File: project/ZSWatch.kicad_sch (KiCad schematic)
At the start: 34 parts, among them IC1 nPM1300-QEXX, IC2 TS3USB221A, IC3 AT25SL128A, M1 NORA-B106, X1 DOCK, X2 INT, X3 VBAT, X4 VBUS, X5 SEL, X6 3V3

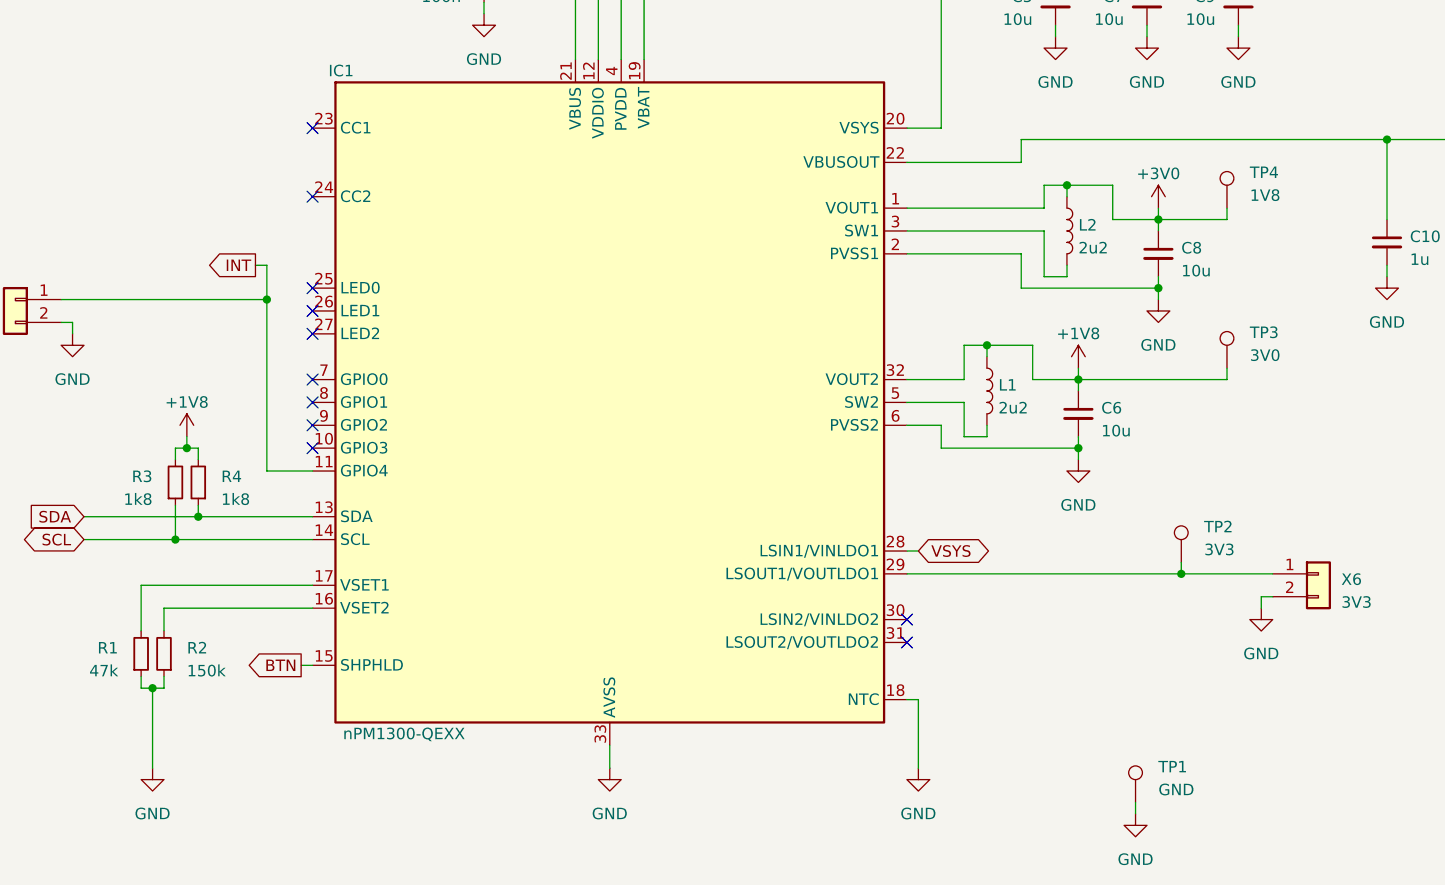
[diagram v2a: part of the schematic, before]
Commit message: Add missing output capacitor for LDO output
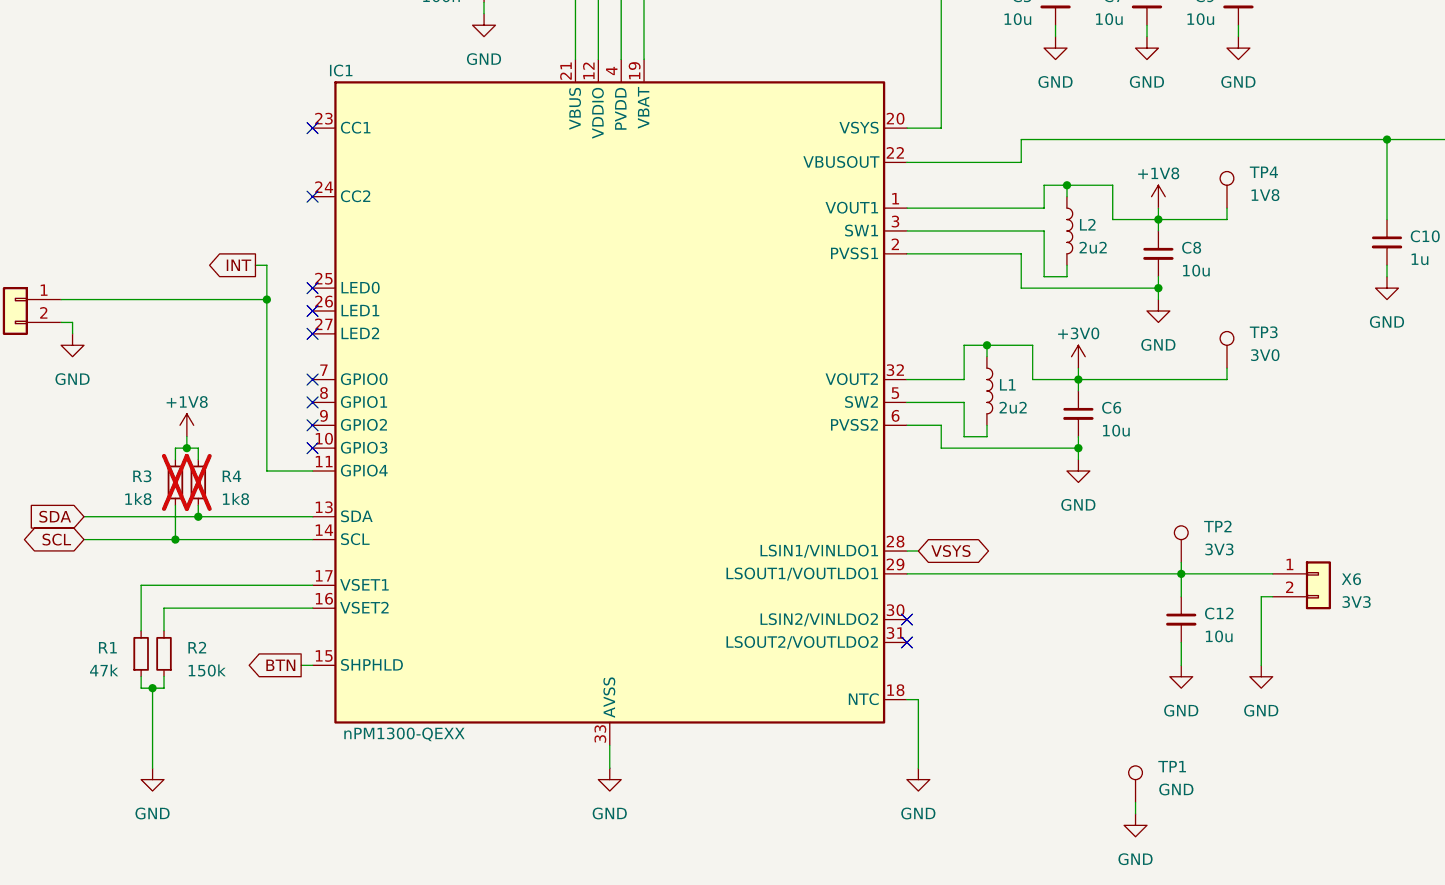
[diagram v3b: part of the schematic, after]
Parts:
- added C12: 10u, Capacitor_SMD:C_0603_1608Metric, symbol Device:C_Small
- R3, R4: now not fitted; now left out of the parts list
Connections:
- net +1V8: now also C8.1, IC1.1 (VOUT1), L2.1, TP4.1; no longer C6.1, IC1.32 (VOUT2), L1.1, TP3.1
- net +3V0: now also C6.1, IC1.32 (VOUT2), L1.1, TP3.1; no longer C8.1, IC1.1 (VOUT1), L2.1, TP4.1
- net GND: now also C12.2
- net at IC1.29 (LSOUT1/VOUTLDO1), TP2.1, X6.1 (Pin_1): now also C12.1
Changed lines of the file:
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@@
     (stroke (width 0) (type default))
   )
-  (wire (pts (xy 161.29 170.18) (xy 161.29 171.45))
+  (wire (pts (xy 161.29 170.18) (xy 161.29 177.8))
     (stroke (width 0) (type default))
   )
@@
     (stroke (width 0) (type default))
   )
+  (wire (pts (xy 152.4 167.64) (xy 152.4 170.18))
+    (stroke (width 0) (type default))
+  )
   (wire (pts (xy 30.48 311.15) (xy 31.75 311.15))
     (stroke (width 0) (type default))
@@
     (stroke (width 0) (type default))
   )
+  (wire (pts (xy 152.4 175.26) (xy 152.4 177.8))
+    (stroke (width 0) (type default))
+  )
   (wire (pts (xy 74.93 96.52) (xy 74.93 97.79))
     (stroke (width 0) (type default))
@@
     )
   )
-  (symbol (lib_id "power:+1V8") (at 140.97 144.78 0) (unit 1)
+  (symbol (lib_id "power:GND") (at 152.4 177.8 0) (unit 1)
+    (in_bom yes) (on_board yes) (dnp no)
+    (property "Reference" "#PWR029" (at 152.4 184.15 0)
+      (effects (font (size 1.27 1.27)) hide)
+    )
+    (property "Value" "GND" (at 152.4 182.88 0)
+      (effects (font (size 1.27 1.27)))
+    )
+    (property "Footprint" "" (at 152.4 177.8 0)
+      (effects (font (size 1.27 1.27)) hide)
+    )
+    (property "Datasheet" "" (at 152.4 177.8 0)
+      (effects (font (size 1.27 1.27)) hide)
+    )
+    (property "Mfr." "" (at 152.4 177.8 0)
+      (effects (font (size 1.27 1.27)) hide)
+    )
+    (property "Mfr. No." "" (at 152.4 177.8 0)
+      (effects (font (size 1.27 1.27)) hide)
+    )
+    (property "Distributor" "" (at 152.4 177.8 0)
+      (effects (font (size 1.27 1.27)) hide)
+    )
+    (property "Order Number" "" (at 152.4 177.8 0)
+      (effects (font (size 1.27 1.27)) hide)
+    )
+    (pin "1")
+    (instances
+      (project "ZSWatch"
+        (path "/d5742f03-3b1a-42e5-a384-018bd4b919aa"
+          (reference "#PWR029") (unit 1)
+        )
+      )
+    )
+  )
+  (symbol (lib_id "power:+1V8") (at 149.86 127 0) (unit 1)
     (in_bom yes) (on_board yes) (dnp no) (fields_autoplaced)
-    (property "Reference" "#PWR019" (at 140.97 148.59 0)
+    (property "Reference" "#PWR019" (at 149.86 130.81 0)
       (effects (font (size 1.27 1.27)) hide)
     )
-    (property "Value" "+1V8" (at 140.97 140.97 0)
+    (property "Value" "+1V8" (at 149.86 123.19 0)
       (effects (font (size 1.27 1.27)))
     )
-    (property "Footprint" "" (at 140.97 144.78 0)
+    (property "Footprint" "" (at 149.86 127 0)
       (effects (font (size 1.27 1.27)) hide)
     )
-    (property "Datasheet" "" (at 140.97 144.78 0)
+    (property "Datasheet" "" (at 149.86 127 0)
       (effects (font (size 1.27 1.27)) hide)
     )
@@
     )
   )
+  (symbol (lib_id "Device:C_Small") (at 152.4 172.72 0) (mirror y) (unit 1)
+    (in_bom yes) (on_board yes) (dnp no) (fields_autoplaced)
+    (property "Reference" "C12" (at 154.94 172.0913 0)
+      (effects (font (size 1.27 1.27)) (justify right))
+    )
+    (property "Value" "10u" (at 154.94 174.6313 0)
+      (effects (font (size 1.27 1.27)) (justify right))
+    )
+    (property "Footprint" "Capacitor_SMD:C_0603_1608Metric" (at 152.4 172.72 0)
+      (effects (font (size 1.27 1.27)) hide)
+    )
+    (property "Datasheet" "https://www.mouser.de/datasheet/2/40/CM_Series_e-2835982.pdf" (at 152.4 172.72 0)
+      (effects (font (size 1.27 1.27)) hide)
+    )
+    (property "Mfr." "KYOCERA AVX" (at 152.4 172.72 0)
+      (effects (font (size 1.27 1.27)) hide)
+    )
+    (property "Mfr. No." "CM105X5R106M25AT" (at 152.4 172.72 0)
+      (effects (font (size 1.27 1.27)) hide)
+    )
+    (property "Distributor" "Mouser" (at 152.4 172.72 0)
+      (effects (font (size 1.27 1.27)) hide)
+    )
+    (property "Order Number" "346-CM105X5R106M25AT" (at 152.4 172.72 0)
+      (effects (font (size 1.27 1.27)) hide)
+    )
+    (pin "1")
+    (pin "2")
+    (instances
+      (project "ZSWatch"
+        (path "/d5742f03-3b1a-42e5-a384-018bd4b919aa"
+          (reference "C12") (unit 1)
+        )
+      )
+    )
+  )
   (symbol (lib_id "Device:C_Small") (at 138.43 104.14 0) (unit 1)
     (in_bom yes) (on_board yes) (dnp no)
@@
     )
   )
-  (symbol (lib_id "power:GND") (at 161.29 171.45 0) (unit 1)
+  (symbol (lib_id "power:GND") (at 161.29 177.8 0) (unit 1)
     (in_bom yes) (on_board yes) (dnp no)
-    (property "Reference" "#PWR026" (at 161.29 177.8 0)
+    (property "Reference" "#PWR026" (at 161.29 184.15 0)
       (effects (font (size 1.27 1.27)) hide)
     )
-    (property "Value" "GND" (at 161.29 176.53 0)
+    (property "Value" "GND" (at 161.29 182.88 0)
       (effects (font (size 1.27 1.27)))
     )
-    (property "Footprint" "" (at 161.29 171.45 0)
+    (property "Footprint" "" (at 161.29 177.8 0)
       (effects (font (size 1.27 1.27)) hide)
     )
-    (property "Datasheet" "" (at 161.29 171.45 0)
+    (property "Datasheet" "" (at 161.29 177.8 0)
       (effects (font (size 1.27 1.27)) hide)
     )
-    (property "Mfr." "" (at 161.29 171.45 0)
+    (property "Mfr." "" (at 161.29 177.8 0)
       (effects (font (size 1.27 1.27)) hide)
     )
-    (property "Mfr. No." "" (at 161.29 171.45 0)
+    (property "Mfr. No." "" (at 161.29 177.8 0)
       (effects (font (size 1.27 1.27)) hide)
     )
-    (property "Distributor" "" (at 161.29 171.45 0)
+    (property "Distributor" "" (at 161.29 177.8 0)
       (effects (font (size 1.27 1.27)) hide)
     )
-    (property "Order Number" "" (at 161.29 171.45 0)
+    (property "Order Number" "" (at 161.29 177.8 0)
       (effects (font (size 1.27 1.27)) hide)
     )
@@
   )
   (symbol (lib_id "Device:R_Small") (at 40.64 157.48 0) (mirror x) (unit 1)
-    (in_bom yes) (on_board yes) (dnp no)
+    (in_bom no) (on_board yes) (dnp yes)
     (property "Reference" "R3" (at 38.1 156.845 0)
       (effects (font (size 1.27 1.27)) (justify right))
@@
     )
   )
-  (symbol (lib_id "power:+3V0") (at 149.86 127 0) (unit 1)
+  (symbol (lib_id "power:+3V0") (at 140.97 144.78 0) (unit 1)
     (in_bom yes) (on_board yes) (dnp no) (fields_autoplaced)
-    (property "Reference" "#PWR023" (at 149.86 130.81 0)
+    (property "Reference" "#PWR023" (at 140.97 148.59 0)
       (effects (font (size 1.27 1.27)) hide)
     )
-    (property "Value" "+3V0" (at 149.86 123.19 0)
+    (property "Value" "+3V0" (at 140.97 140.97 0)
       (effects (font (size 1.27 1.27)))
     )
-    (property "Footprint" "" (at 149.86 127 0)
+    (property "Footprint" "" (at 140.97 144.78 0)
       (effects (font (size 1.27 1.27)) hide)
     )
-    (property "Datasheet" "" (at 149.86 127 0)
+    (property "Datasheet" "" (at 140.97 144.78 0)
       (effects (font (size 1.27 1.27)) hide)
     )
@@
   )
   (symbol (lib_id "Device:R_Small") (at 43.18 157.48 180) (unit 1)
-    (in_bom yes) (on_board yes) (dnp no) (fields_autoplaced)
+    (in_bom no) (on_board yes) (dnp yes) (fields_autoplaced)
     (property "Reference" "R4" (at 45.72 156.845 0)
       (effects (font (size 1.27 1.27)) (justify right))
